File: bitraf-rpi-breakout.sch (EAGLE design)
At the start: 20 parts, among them IC1 74HC595N, K1 JS-M1-9V-4, T1 BC547

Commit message: Rev b.
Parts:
- D1, D2: value (none) -> 3.3V
- D3: value 1N4148DO35-7 -> 1N4004; device diode:1N4148DO35-7 -> diode:1N4004
- R1, R2, R3, R4: value (none) -> 330
- R6, R7: value (none) -> 4.7k
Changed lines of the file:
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@@
 <part name="T1" library="transistor" deviceset="BC547" device=""/>
 <part name="K1" library="relay" deviceset="JS-M1*" device="" technology="-9V-4"/>
-<part name="R1" library="resistor" deviceset="R-EU_" device="0204/7"/>
-<part name="R2" library="resistor" deviceset="R-EU_" device="0204/7"/>
-<part name="R3" library="eagle-ltspice" deviceset="R" device="R1206"/>
-<part name="R4" library="eagle-ltspice" deviceset="R" device="R1206"/>
-<part name="D1" library="diode" deviceset="ZENER-DIODE" device="ZD-7.5"/>
-<part name="D2" library="diode" deviceset="ZENER-DIODE" device="ZD-7.5"/>
+<part name="R1" library="resistor" deviceset="R-EU_" device="0204/7" value="330"/>
+<part name="R2" library="resistor" deviceset="R-EU_" device="0204/7" value="330"/>
+<part name="R3" library="eagle-ltspice" deviceset="R" device="R1206" value="330"/>
+<part name="R4" library="eagle-ltspice" deviceset="R" device="R1206" value="330"/>
+<part name="D1" library="diode" deviceset="ZENER-DIODE" device="ZD-7.5" value="3.3V"/>
+<part name="D2" library="diode" deviceset="ZENER-DIODE" device="ZD-7.5" value="3.3V"/>
 <part name="LED1" library="led" deviceset="LED" device="3MM"/>
 <part name="LED2" library="led" deviceset="LED" device="3MM"/>
@@
 <part name="R5" library="resistor" deviceset="R-EU_" device="0204/7" value="1k"/>
 <part name="GND2" library="supply1" deviceset="GND" device=""/>
-<part name="R6" library="resistor" deviceset="R-EU_" device="0204/7"/>
-<part name="R7" library="resistor" deviceset="R-EU_" device="0204/7"/>
+<part name="R6" library="resistor" deviceset="R-EU_" device="0204/7" value="4.7k"/>
+<part name="R7" library="resistor" deviceset="R-EU_" device="0204/7" value="4.7k"/>
 <part name="SUPPLY1" library="supply2" deviceset="VCC" device=""/>
-<part name="D3" library="diode" deviceset="1N4148" device="DO35-7"/>
+<part name="D3" library="diode" deviceset="1N4004" device=""/>
 <part name="SUPPLY2" library="supply2" deviceset="VCC" device=""/>
 <part name="SV1" library="con-ml" deviceset="ML26" device=""/>
@@
 <instance part="R7" gate="G$1" x="35.56" y="45.72" rot="R270"/>
 <instance part="SUPPLY1" gate="G$1" x="160.02" y="101.6"/>
-<instance part="D3" gate="G$1" x="147.32" y="60.96" rot="R90"/>
+<instance part="D3" gate="1" x="147.32" y="60.96" rot="R90"/>
 <instance part="SUPPLY2" gate="G$1" x="12.7" y="99.06"/>
 <instance part="SV1" gate="1" x="0" y="73.66" rot="R180"/>
@@
 <pinref part="T1" gate="G$1" pin="C"/>
 <wire x1="160.02" y1="55.88" x2="160.02" y2="53.34" width="0.1524" layer="91"/>
-<pinref part="D3" gate="G$1" pin="A"/>
+<pinref part="D3" gate="1" pin="A"/>
 <wire x1="160.02" y1="53.34" x2="160.02" y2="40.64" width="0.1524" layer="91"/>
 <wire x1="160.02" y1="53.34" x2="147.32" y2="53.34" width="0.1524" layer="91"/>
@@
 <wire x1="160.02" y1="66.04" x2="160.02" y2="71.12" width="0.1524" layer="91"/>
 <pinref part="SUPPLY1" gate="G$1" pin="VCC"/>
-<pinref part="D3" gate="G$1" pin="C"/>
+<pinref part="D3" gate="1" pin="C"/>
 <wire x1="160.02" y1="71.12" x2="160.02" y2="99.06" width="0.1524" layer="91"/>
 <wire x1="147.32" y1="63.5" x2="147.32" y2="71.12" width="0.1524" layer="91"/>

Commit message: nits
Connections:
- net GND: no longer IC1A.SCL
- net VCC: now also IC1A.SCL
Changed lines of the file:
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@@
 <grid distance="0.1" unitdist="inch" unit="inch" style="lines" multiple="1" display="no" altdistance="0.01" altunitdist="inch" altunit="inch"/>
 <layers>
-<layer number="1" name="Top" color="4" fill="1" visible="yes" active="no"/>
-<layer number="16" name="Bottom" color="1" fill="1" visible="yes" active="no"/>
-<layer number="17" name="Pads" color="2" fill="1" visible="yes" active="no"/>
-<layer number="18" name="Vias" color="2" fill="1" visible="yes" active="no"/>
-<layer number="19" name="Unrouted" color="6" fill="1" visible="yes" active="no"/>
-<layer number="20" name="Dimension" color="15" fill="1" visible="yes" active="no"/>
-<layer number="21" name="tPlace" color="7" fill="1" visible="yes" active="no"/>
-<layer number="22" name="bPlace" color="7" fill="1" visible="yes" active="no"/>
-<layer number="23" name="tOrigins" color="15" fill="1" visible="yes" active="no"/>
-<layer number="24" name="bOrigins" color="15" fill="1" visible="yes" active="no"/>
-<layer number="25" name="tNames" color="7" fill="1" visible="yes" active="no"/>
-<layer number="26" name="bNames" color="7" fill="1" visible="yes" active="no"/>
-<layer number="27" name="tValues" color="7" fill="1" visible="yes" active="no"/>
-<layer number="28" name="bValues" color="7" fill="1" visible="yes" active="no"/>
+<layer number="1" name="Top" color="4" fill="1" visible="no" active="no"/>
+<layer number="16" name="Bottom" color="1" fill="1" visible="no" active="no"/>
+<layer number="17" name="Pads" color="2" fill="1" visible="no" active="no"/>
+<layer number="18" name="Vias" color="2" fill="1" visible="no" active="no"/>
+<layer number="19" name="Unrouted" color="6" fill="1" visible="no" active="no"/>
+<layer number="20" name="Dimension" color="15" fill="1" visible="no" active="no"/>
+<layer number="21" name="tPlace" color="7" fill="1" visible="no" active="no"/>
+<layer number="22" name="bPlace" color="7" fill="1" visible="no" active="no"/>
+<layer number="23" name="tOrigins" color="15" fill="1" visible="no" active="no"/>
+<layer number="24" name="bOrigins" color="15" fill="1" visible="no" active="no"/>
+<layer number="25" name="tNames" color="7" fill="1" visible="no" active="no"/>
+<layer number="26" name="bNames" color="7" fill="1" visible="no" active="no"/>
+<layer number="27" name="tValues" color="7" fill="1" visible="no" active="no"/>
+<layer number="28" name="bValues" color="7" fill="1" visible="no" active="no"/>
 <layer number="29" name="tStop" color="7" fill="3" visible="no" active="no"/>
 <layer number="30" name="bStop" color="7" fill="6" visible="no" active="no"/>
@@
 <layer number="35" name="tGlue" color="7" fill="4" visible="no" active="no"/>
 <layer number="36" name="bGlue" color="7" fill="5" visible="no" active="no"/>
-<layer number="37" name="tTest" color="7" fill="1" visible="yes" active="no"/>
-<layer number="38" name="bTest" color="7" fill="1" visible="yes" active="no"/>
+<layer number="37" name="tTest" color="7" fill="1" visible="no" active="no"/>
+<layer number="38" name="bTest" color="7" fill="1" visible="no" active="no"/>
 <layer number="39" name="tKeepout" color="4" fill="11" visible="no" active="no"/>
 <layer number="40" name="bKeepout" color="1" fill="11" visible="no" active="no"/>
@@
 <layer number="44" name="Drills" color="7" fill="1" visible="no" active="no"/>
 <layer number="45" name="Holes" color="7" fill="1" visible="no" active="no"/>
-<layer number="46" name="Milling" color="3" fill="1" visible="yes" active="no"/>
-<layer number="47" name="Measures" color="7" fill="1" visible="yes" active="no"/>
-<layer number="48" name="Document" color="7" fill="1" visible="yes" active="no"/>
-<layer number="49" name="Reference" color="7" fill="1" visible="yes" active="no"/>
-<layer number="51" name="tDocu" color="7" fill="1" visible="yes" active="no"/>
-<layer number="52" name="bDocu" color="7" fill="1" visible="yes" active="no"/>
+<layer number="46" name="Milling" color="3" fill="1" visible="no" active="no"/>
+<layer number="47" name="Measures" color="7" fill="1" visible="no" active="no"/>
+<layer number="48" name="Document" color="7" fill="1" visible="no" active="no"/>
+<layer number="49" name="Reference" color="7" fill="1" visible="no" active="no"/>
+<layer number="51" name="tDocu" color="7" fill="1" visible="no" active="no"/>
+<layer number="52" name="bDocu" color="7" fill="1" visible="no" active="no"/>
 <layer number="91" name="Nets" color="2" fill="1" visible="yes" active="yes"/>
 <layer number="92" name="Busses" color="1" fill="1" visible="yes" active="yes"/>
@@
 </class>
 <class number="1" name="power" width="1" drill="0">
+<clearance class="1" value="0.355"/>
 </class>
 </classes>
@@
 <part name="J1" library="con-amp" deviceset="MTA03-156" device=""/>
 <part name="SUPPLY3" library="supply2" deviceset="VCC" device=""/>
+<part name="SUPPLY4" library="supply2" deviceset="VCC" device=""/>
 </parts>
 <sheets>
@@
 <instance part="J1" gate="G$2" x="208.28" y="63.5" rot="R270"/>
 <instance part="SUPPLY3" gate="G$1" x="78.74" y="48.26"/>
+<instance part="SUPPLY4" gate="G$1" x="50.8" y="99.06"/>
 </instances>
 <busses>
@@
 </segment>
 <segment>
-<pinref part="IC1" gate="A" pin="SCL"/>
-<wire x1="55.88" y1="86.36" x2="50.8" y2="86.36" width="0.1524" layer="91"/>
-<wire x1="50.8" y1="86.36" x2="50.8" y2="71.12" width="0.1524" layer="91"/>
 <pinref part="IC1" gate="A" pin="G"/>
 <wire x1="50.8" y1="71.12" x2="50.8" y2="68.58" width="0.1524" layer="91"/>
 <wire x1="55.88" y1="71.12" x2="50.8" y2="71.12" width="0.1524" layer="91"/>
-<junction x="50.8" y="71.12"/>
 <pinref part="GND4" gate="1" pin="GND"/>
 </segment>
@@
 <segment>
 <pinref part="K1" gate="1" pin="1"/>
-<wire x1="160.02" y1="66.04" x2="160.02" y2="71.12" width="0.1524" layer="91"/>
+<wire x1="160.02" y1="66.04" x2="160.02" y2="68.58" width="0.1524" layer="91"/>
 <pinref part="SUPPLY1" gate="G$1" pin="VCC"/>
 <pinref part="D3" gate="1" pin="C"/>
-<wire x1="160.02" y1="71.12" x2="160.02" y2="99.06" width="0.1524" layer="91"/>
-<wire x1="147.32" y1="63.5" x2="147.32" y2="71.12" width="0.1524" layer="91"/>
-<wire x1="147.32" y1="71.12" x2="160.02" y2="71.12" width="0.1524" layer="91"/>
-<junction x="160.02" y="71.12"/>
+<wire x1="160.02" y1="68.58" x2="160.02" y2="99.06" width="0.1524" layer="91"/>
+<wire x1="147.32" y1="63.5" x2="147.32" y2="68.58" width="0.1524" layer="91"/>
+<wire x1="147.32" y1="68.58" x2="160.02" y2="68.58" width="0.1524" layer="91"/>
+<junction x="160.02" y="68.58"/>
 </segment>
 <segment>
@@
 <pinref part="SUPPLY3" gate="G$1" pin="VCC"/>
 </segment>
-</net>
+<segment>
+<pinref part="IC1" gate="A" pin="SCL"/>
+<wire x1="55.88" y1="86.36" x2="50.8" y2="86.36" width="0.1524" layer="91"/>
+<pinref part="SUPPLY4" gate="G$1" pin="VCC"/>
+<wire x1="50.8" y1="86.36" x2="50.8" y2="96.52" width="0.1524" layer="91"/>
+</segment>
+</net>

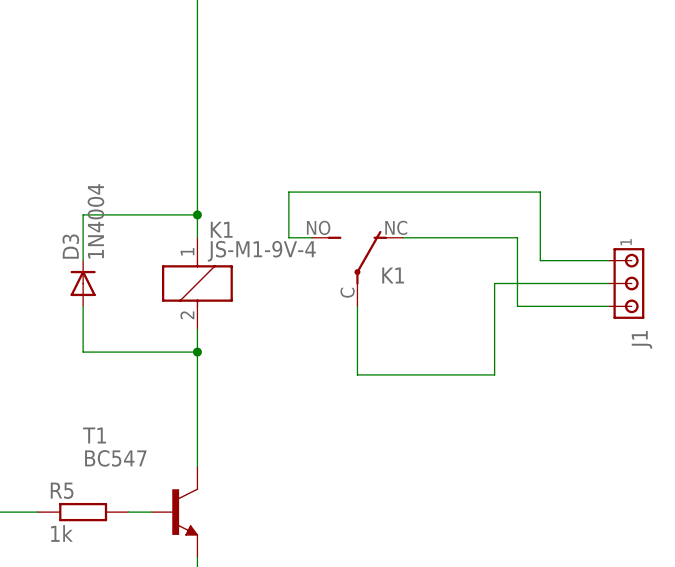
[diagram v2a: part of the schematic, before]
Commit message: o Changing relay.
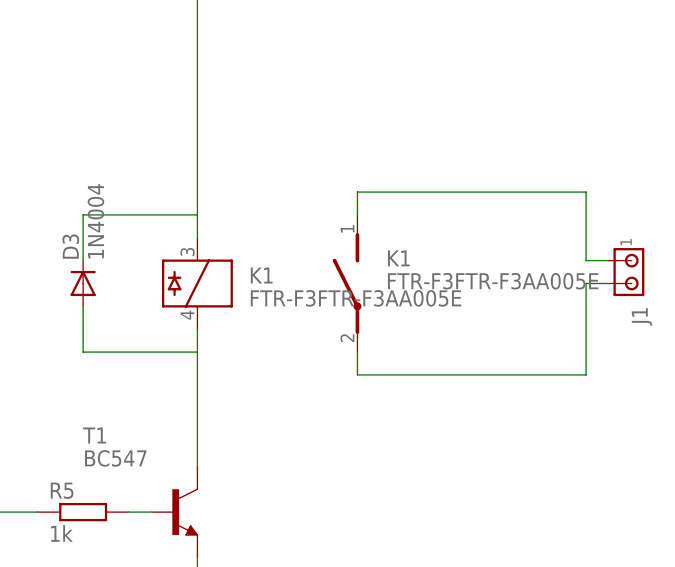
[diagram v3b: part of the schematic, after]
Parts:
- J1: device con-amp:MTA03-156 -> con-amp:MTA02-156
- K1: value JS-M1-9V-4 -> FTR-F3FTR-F3AA005E; device relay:JS-M1-9V-4 -> fujitsu-ftr-f3:FTR-F3FTR-F3AA005E
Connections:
- removed net N$18: J1.3, K12.O
- net N$15: now also K11.4; no longer K11.2
- net N$16: now also K12.2; no longer K12.P
- net N$17: now also K12.1; no longer K12.S
- net VCC: now also K11.3; no longer K11.1
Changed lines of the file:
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@@
 <part name="IC1" library="74xx-eu" deviceset="74*595" device="N" technology="HC"/>
 <part name="T1" library="transistor" deviceset="BC547" device=""/>
-<part name="K1" library="relay" deviceset="JS-M1*" device="" technology="-9V-4"/>
 <part name="R1" library="resistor" deviceset="R-EU_" device="0204/7" value="330"/>
 <part name="R2" library="resistor" deviceset="R-EU_" device="0204/7" value="330"/>
@@
 <part name="GND4" library="supply1" deviceset="GND" device=""/>
 <part name="JP1" library="pinhead" deviceset="PINHD-2X2" device=""/>
-<part name="J1" library="con-amp" deviceset="MTA03-156" device=""/>
+<part name="J1" library="con-amp" deviceset="MTA02-156" device=""/>
 <part name="SUPPLY3" library="supply2" deviceset="VCC" device=""/>
 <part name="SUPPLY4" library="supply2" deviceset="VCC" device=""/>
+<part name="K1" library="fujitsu-ftr-f3" deviceset="FTR-F3" device="" technology="FTR-F3AA005E"/>
 </parts>
 <sheets>
@@
 <instance part="IC1" gate="A" x="68.58" y="83.82"/>
 <instance part="T1" gate="G$1" x="157.48" y="35.56"/>
-<instance part="K1" gate="1" x="160.02" y="60.96"/>
-<instance part="K1" gate="2" x="177.8" y="60.96"/>
 <instance part="R1" gate="G$1" x="99.06" y="48.26" rot="R270"/>
 <instance part="R2" gate="G$1" x="88.9" y="48.26" rot="R270"/>
@@
 <instance part="GND4" gate="1" x="50.8" y="66.04"/>
 <instance part="JP1" gate="A" x="66.04" y="38.1"/>
-<instance part="J1" gate="G$2" x="208.28" y="63.5" rot="R270"/>
+<instance part="J1" gate="G$1" x="208.28" y="63.5" rot="R270"/>
 <instance part="SUPPLY3" gate="G$1" x="78.74" y="48.26"/>
 <instance part="SUPPLY4" gate="G$1" x="50.8" y="99.06"/>
+<instance part="K1" gate="1" x="160.02" y="60.96"/>
+<instance part="K1" gate="2" x="177.8" y="60.96"/>
 </instances>
 <busses>
@@
 <net name="N$15" class="0">
 <segment>
-<pinref part="K1" gate="1" pin="2"/>
 <pinref part="T1" gate="G$1" pin="C"/>
-<wire x1="160.02" y1="55.88" x2="160.02" y2="53.34" width="0.1524" layer="91"/>
 <pinref part="D3" gate="1" pin="A"/>
 <wire x1="160.02" y1="53.34" x2="160.02" y2="40.64" width="0.1524" layer="91"/>
 <wire x1="160.02" y1="53.34" x2="147.32" y2="53.34" width="0.1524" layer="91"/>
 <wire x1="147.32" y1="53.34" x2="147.32" y2="58.42" width="0.1524" layer="91"/>
-<junction x="160.02" y="53.34"/>
+<pinref part="K1" gate="1" pin="4"/>
+<wire x1="160.02" y1="53.34" x2="160.02" y2="55.88" width="0.1524" layer="91"/>
 </segment>
 </net>
 <net name="N$16" class="1">
 <segment>
-<pinref part="K1" gate="2" pin="P"/>
-<wire x1="177.8" y1="58.42" x2="177.8" y2="50.8" width="0.1524" layer="91"/>
-<wire x1="177.8" y1="50.8" x2="193.04" y2="50.8" width="0.1524" layer="91"/>
-<wire x1="193.04" y1="60.96" x2="193.04" y2="50.8" width="0.1524" layer="91"/>
-<pinref part="J1" gate="G$2" pin="2"/>
-<wire x1="205.74" y1="60.96" x2="193.04" y2="60.96" width="0.1524" layer="91"/>
+<wire x1="177.8" y1="50.8" x2="203.2" y2="50.8" width="0.1524" layer="91"/>
+<pinref part="K1" gate="2" pin="2"/>
+<wire x1="177.8" y1="53.34" x2="177.8" y2="50.8" width="0.1524" layer="91"/>
+<wire x1="203.2" y1="50.8" x2="203.2" y2="60.96" width="0.1524" layer="91"/>
+<pinref part="J1" gate="G$1" pin="2"/>
+<wire x1="203.2" y1="60.96" x2="205.74" y2="60.96" width="0.1524" layer="91"/>
 </segment>
 </net>
 <net name="N$17" class="1">
 <segment>
-<pinref part="K1" gate="2" pin="S"/>
-<wire x1="172.72" y1="66.04" x2="170.18" y2="66.04" width="0.1524" layer="91"/>
-<wire x1="170.18" y1="66.04" x2="170.18" y2="71.12" width="0.1524" layer="91"/>
-<wire x1="170.18" y1="71.12" x2="198.12" y2="71.12" width="0.1524" layer="91"/>
-<wire x1="198.12" y1="71.12" x2="198.12" y2="63.5" width="0.1524" layer="91"/>
-<wire x1="198.12" y1="63.5" x2="205.74" y2="63.5" width="0.1524" layer="91"/>
-<pinref part="J1" gate="G$2" pin="1"/>
-</segment>
-</net>
-<net name="N$18" class="1">
-<segment>
-<pinref part="K1" gate="2" pin="O"/>
-<wire x1="182.88" y1="66.04" x2="195.58" y2="66.04" width="0.1524" layer="91"/>
-<pinref part="J1" gate="G$2" pin="3"/>
-<wire x1="205.74" y1="58.42" x2="195.58" y2="58.42" width="0.1524" layer="91"/>
-<wire x1="195.58" y1="58.42" x2="195.58" y2="66.04" width="0.1524" layer="91"/>
+<pinref part="J1" gate="G$1" pin="1"/>
+<wire x1="177.8" y1="71.12" x2="203.2" y2="71.12" width="0.1524" layer="91"/>
+<wire x1="205.74" y1="63.5" x2="203.2" y2="63.5" width="0.1524" layer="91"/>
+<wire x1="203.2" y1="63.5" x2="203.2" y2="71.12" width="0.1524" layer="91"/>
+<pinref part="K1" gate="2" pin="1"/>
+<wire x1="177.8" y1="68.58" x2="177.8" y2="71.12" width="0.1524" layer="91"/>
 </segment>
 </net>
 <net name="VCC" class="0">
 <segment>
-<pinref part="K1" gate="1" pin="1"/>
-<wire x1="160.02" y1="66.04" x2="160.02" y2="68.58" width="0.1524" layer="91"/>
 <pinref part="SUPPLY1" gate="G$1" pin="VCC"/>
 <pinref part="D3" gate="1" pin="C"/>
@@
 <wire x1="147.32" y1="63.5" x2="147.32" y2="68.58" width="0.1524" layer="91"/>
 <wire x1="147.32" y1="68.58" x2="160.02" y2="68.58" width="0.1524" layer="91"/>
-<junction x="160.02" y="68.58"/>
-</segment>
-<segment>
+<pinref part="K1" gate="1" pin="3"/>
+<wire x1="160.02" y1="68.58" x2="160.02" y2="66.04" width="0.1524" layer="91"/>
+</segment>
+<segment>

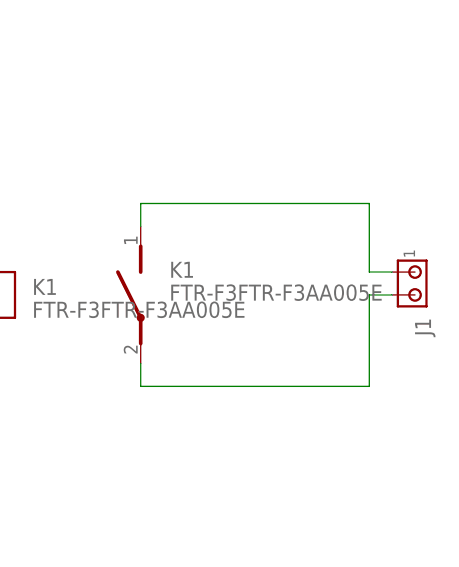
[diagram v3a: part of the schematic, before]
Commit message: o Relay was upside down.
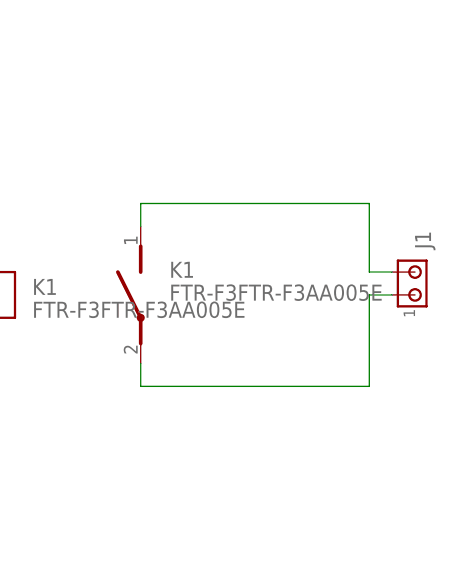
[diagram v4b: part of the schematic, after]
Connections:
- net N$16: now also J1.1; no longer J1.2
- net N$17: now also J1.2; no longer J1.1
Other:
- moved on the sheet: J1
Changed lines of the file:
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@@
 <instance part="GND4" gate="1" x="50.8" y="66.04"/>
 <instance part="JP1" gate="A" x="66.04" y="38.1"/>
-<instance part="J1" gate="G$1" x="208.28" y="63.5" rot="R270"/>
+<instance part="J1" gate="G$1" x="208.28" y="60.96" rot="MR90"/>
 <instance part="SUPPLY3" gate="G$1" x="78.74" y="48.26"/>
 <instance part="SUPPLY4" gate="G$1" x="50.8" y="99.06"/>
@@
 <wire x1="177.8" y1="53.34" x2="177.8" y2="50.8" width="0.1524" layer="91"/>
 <wire x1="203.2" y1="50.8" x2="203.2" y2="60.96" width="0.1524" layer="91"/>
-<pinref part="J1" gate="G$1" pin="2"/>
-<wire x1="203.2" y1="60.96" x2="205.74" y2="60.96" width="0.1524" layer="91"/>
+<pinref part="J1" gate="G$1" pin="1"/>
+<wire x1="205.74" y1="60.96" x2="203.2" y2="60.96" width="0.1524" layer="91"/>
 </segment>
 </net>
 <net name="N$17" class="1">
 <segment>
-<pinref part="J1" gate="G$1" pin="1"/>
 <wire x1="177.8" y1="71.12" x2="203.2" y2="71.12" width="0.1524" layer="91"/>
-<wire x1="205.74" y1="63.5" x2="203.2" y2="63.5" width="0.1524" layer="91"/>
 <wire x1="203.2" y1="63.5" x2="203.2" y2="71.12" width="0.1524" layer="91"/>
 <pinref part="K1" gate="2" pin="1"/>
 <wire x1="177.8" y1="68.58" x2="177.8" y2="71.12" width="0.1524" layer="91"/>
-</segment>
-</net>
+<pinref part="J1" gate="G$1" pin="2"/>
+<wire x1="203.2" y1="63.5" x2="205.74" y2="63.5" width="0.1524" layer="91"/>
+</segment>
+</net>
